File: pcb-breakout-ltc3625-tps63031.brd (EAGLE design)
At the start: 40 x 22.7 mm, 16 parts, among them IC1 LTC3625

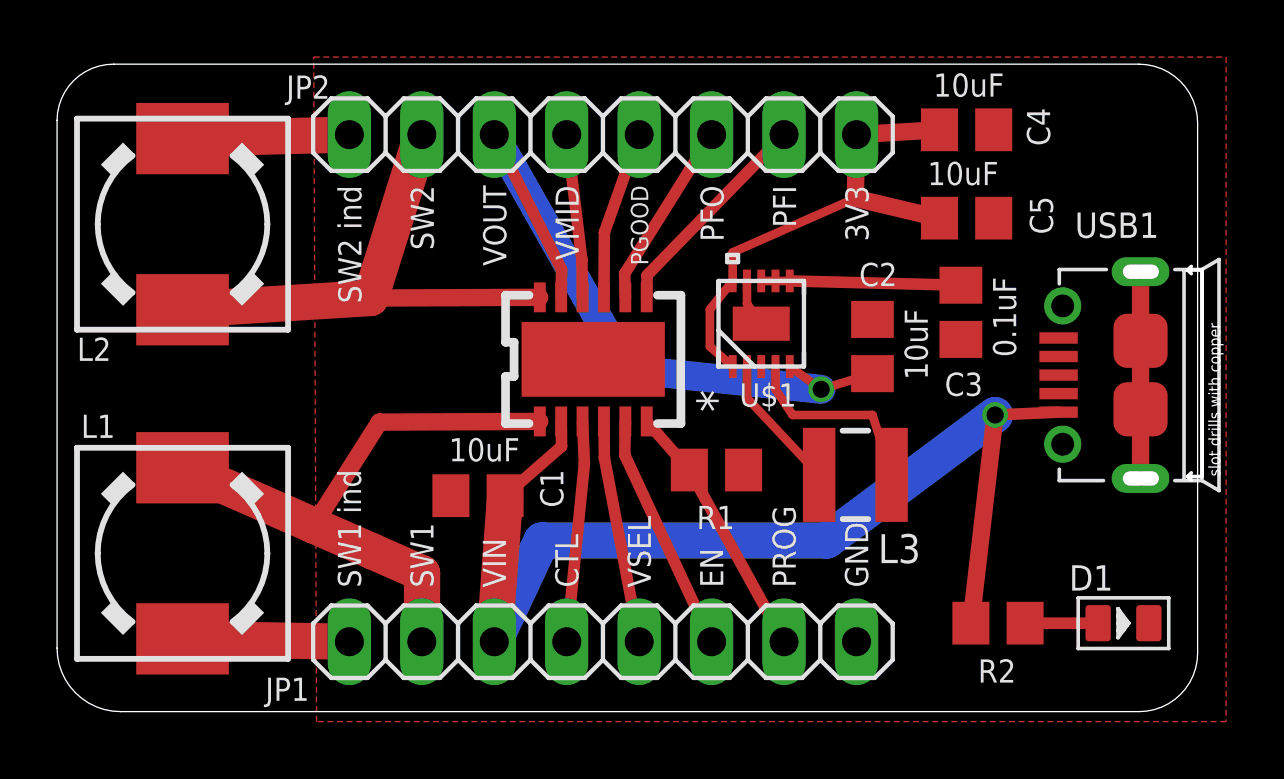
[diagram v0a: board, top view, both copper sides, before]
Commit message: corrected package error in ltc3625 lbr
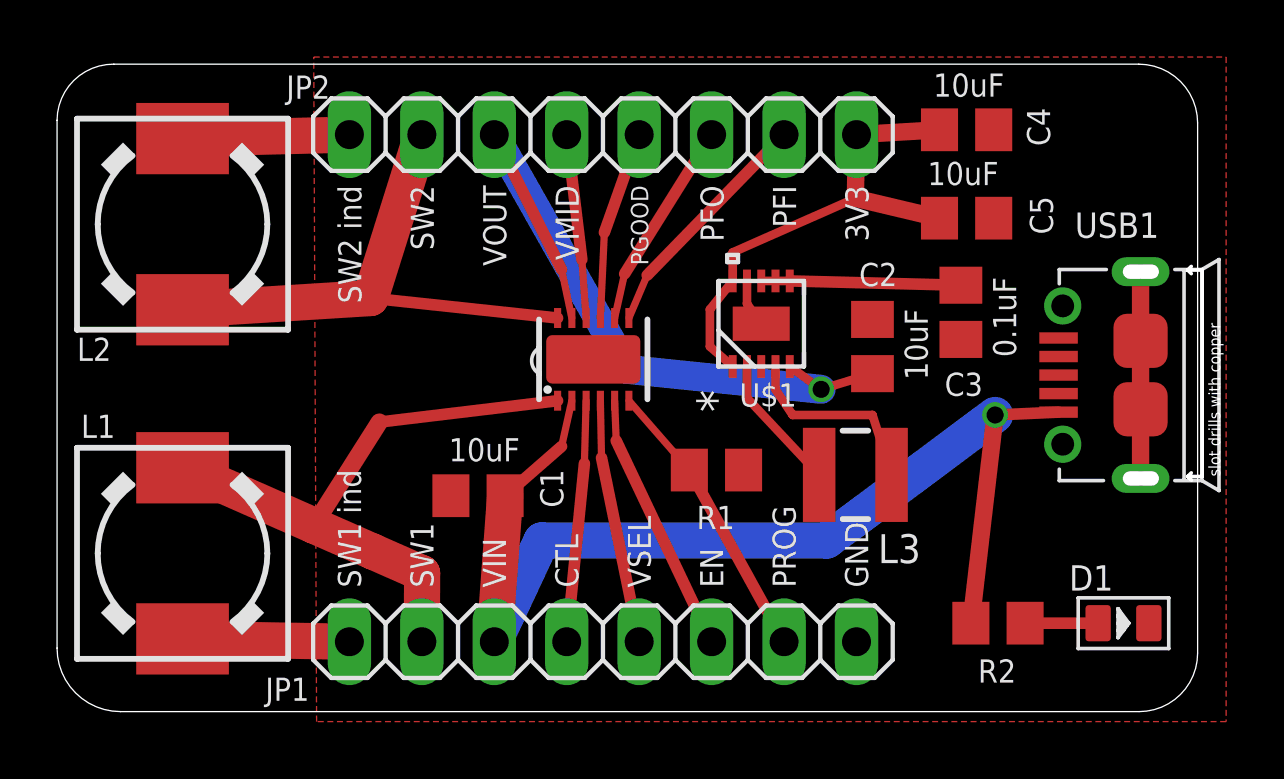
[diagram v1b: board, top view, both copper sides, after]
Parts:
- IC1: value LTC3625 -> LTC3625EDE
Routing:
- net L3625_PROG: track 9.14 -> 10.1 mm
- net L3625_PFI: track 7.66 -> 8.51 mm
- net L3625_EN: track 8.40 -> 9.20 mm
- net L3625_VIN: track 39.5 -> 40.3 mm
- net L3625_PFO: track 6.58 -> 7.34 mm
- net L3625_VOUT: track 25.8 -> 26.6 mm
- net L3625_VSEL: track 7.84 -> 8.58 mm
- net L3625_VMID: track 5.74 -> 6.47 mm
- net L3625_PGOOD: track 5.92 -> 6.64 mm
- net L3625_CTL: track 7.76 -> 8.48 mm
- net L3625_SW1: track 21.5 -> 22.2 mm
- net L3625_SW2: track 18.5 -> 19.2 mm
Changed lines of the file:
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@@
 <layer number="27" name="tValues" color="7" fill="1" visible="yes" active="yes"/>
 <layer number="28" name="bValues" color="7" fill="1" visible="yes" active="yes"/>
-<layer number="29" name="tStop" color="7" fill="3" visible="yes" active="yes"/>
-<layer number="30" name="bStop" color="7" fill="6" visible="yes" active="yes"/>
+<layer number="29" name="tStop" color="7" fill="3" visible="no" active="yes"/>
+<layer number="30" name="bStop" color="7" fill="6" visible="no" active="yes"/>
 <layer number="31" name="tCream" color="7" fill="4" visible="yes" active="yes"/>
 <layer number="32" name="bCream" color="7" fill="5" visible="yes" active="yes"/>
@@
 </autorouter>
 <elements>
-<element name="IC1" library="ltc3625" package="DFN12(DE)" value="LTC3625" x="18.81" y="12.35" smashed="yes">
+<element name="IC1" library="ltc3625" package="DFN12(DE)" value="LTC3625EDE" x="18.81" y="12.35" smashed="yes">
 <attribute name="NAME" x="14.9" y="12.67" size="1.016" layer="27" rot="R90" align="center"/>
 </element>
@@
 <wire x1="9.010409375" y1="6.523628125" x2="11.081146875" y2="5.61151875" width="1.27" layer="1"/>
 <wire x1="11.081146875" y1="5.61151875" x2="12.81" y2="4.85" width="1.27" layer="1"/>
-<wire x1="16.935" y1="10.175" x2="11.31" y2="10.15" width="0.6096" layer="1"/>
+<wire x1="17.56" y1="10.9" x2="11.31" y2="10.15" width="0.4064" layer="1"/>
 <wire x1="11.31" y1="10.15" x2="9.010409375" y2="6.523628125" width="0.6096" layer="1"/>
 <contactref element="JP1" pad="2"/>
@@
 <contactref element="IC1" pad="4"/>
 <contactref element="JP1" pad="5"/>
-<wire x1="19.185" y1="10.175" x2="19.2" y2="8.9" width="0.4064" layer="1"/>
-<wire x1="19.2" y1="8.9" x2="20.42" y2="2.45" width="0.4064" layer="1"/>
+<wire x1="19.06" y1="10.9" x2="19.1" y2="8.9" width="0.254" layer="1"/>
+<wire x1="19.1" y1="8.9" x2="20.42" y2="2.45" width="0.4064" layer="1"/>
 </signal>
 <signal name="L3625_PROG">
@@
 <contactref element="JP1" pad="7"/>
 <wire x1="22.18" y1="8.47" x2="25.5" y2="2.45" width="0.4064" layer="1"/>
-<wire x1="20.685" y1="10.175" x2="22.18" y2="8.47" width="0.4064" layer="1"/>
+<wire x1="20.06" y1="10.9" x2="22.18" y2="8.47" width="0.254" layer="1"/>
 </signal>
 <signal name="GND">
@@
 <signal name="L3625_EN">
 <contactref element="IC1" pad="5"/>
-<wire x1="19.935" y1="10.175" x2="19.91435" y2="8.99799375" width="0.4064" layer="1"/>
+<wire x1="19.56" y1="10.9" x2="19.61435" y2="9.49799375" width="0.254" layer="1"/>
 <contactref element="JP1" pad="6"/>
-<wire x1="19.91435" y1="8.99799375" x2="22.96" y2="2.45" width="0.4064" layer="1"/>
+<wire x1="19.61435" y1="9.49799375" x2="22.96" y2="2.45" width="0.4064" layer="1"/>
 </signal>
 <signal name="L3625_CTL">
 <contactref element="IC1" pad="3"/>
 <contactref element="JP1" pad="4"/>
-<wire x1="18.435" y1="10.175" x2="18.5" y2="8.7" width="0.4064" layer="1"/>
+<wire x1="18.56" y1="10.9" x2="18.5" y2="8.7" width="0.254" layer="1"/>
 <wire x1="18.5" y1="8.7" x2="17.88" y2="2.45" width="0.4064" layer="1"/>
 </signal>
@@
 <contactref element="JP2" pad="2"/>
 <contactref element="IC1" pad="7"/>
-<wire x1="20.685" y1="14.525" x2="20.7" y2="15.3" width="0.4064" layer="1"/>
+<wire x1="20.06" y1="13.8" x2="20.7" y2="15.3" width="0.254" layer="1"/>
 <wire x1="20.7" y1="15.3" x2="25.5" y2="20.23" width="0.4064" layer="1"/>
 </signal>
@@
 <contactref element="JP2" pad="3"/>
 <contactref element="IC1" pad="8"/>
-<wire x1="19.935" y1="14.525" x2="19.91" y2="15.35" width="0.4064" layer="1"/>
+<wire x1="19.56" y1="13.8" x2="19.91" y2="15.35" width="0.254" layer="1"/>
 <wire x1="19.91" y1="15.35" x2="22.96" y2="20.23" width="0.4064" layer="1"/>
 </signal>
@@
 <contactref element="JP2" pad="4"/>
 <contactref element="IC1" pad="9"/>
-<wire x1="19.185" y1="14.525" x2="19.2" y2="16.8" width="0.4064" layer="1"/>
+<wire x1="19.06" y1="13.8" x2="19.2" y2="16.8" width="0.254" layer="1"/>
 <wire x1="19.2" y1="16.8" x2="20.42" y2="20.23" width="0.4064" layer="1"/>
 </signal>
@@
 <contactref element="JP2" pad="5"/>
 <contactref element="IC1" pad="10"/>
-<wire x1="18.435" y1="14.525" x2="18.41" y2="15.85" width="0.4064" layer="1"/>
+<wire x1="18.56" y1="13.8" x2="18.41" y2="15.85" width="0.254" layer="1"/>
 <wire x1="18.41" y1="15.85" x2="17.88" y2="20.23" width="0.4064" layer="1"/>
 </signal>
@@
 <contactref element="JP2" pad="6"/>
 <contactref element="IC1" pad="11"/>
-<wire x1="17.685" y1="14.525" x2="17.7" y2="15.5" width="0.4064" layer="1"/>
+<wire x1="18.06" y1="13.8" x2="17.7" y2="15.5" width="0.254" layer="1"/>
 <wire x1="17.7" y1="15.5" x2="15.34" y2="20.23" width="0.4064" layer="1"/>
 <contactref element="U$1" pad="5"/>
@@
 <wire x1="4.41" y1="14.09" x2="11" y2="14.5" width="1.27" layer="1"/>
 <wire x1="11" y1="14.5" x2="12.8" y2="20.23" width="1.27" layer="1"/>
-<wire x1="16.935" y1="14.525" x2="11" y2="14.5" width="0.6096" layer="1"/>
+<wire x1="17.56" y1="13.8" x2="11" y2="14.5" width="0.4064" layer="1"/>
 </signal>
 <signal name="L3625_SW2_IND">
@@
 <wire x1="35.125" y1="10.5" x2="32.9" y2="10.4" width="0.4064" layer="1"/>
 <wire x1="15.34" y1="2.45" x2="15.72" y2="7.57" width="1.27" layer="1"/>
-<wire x1="17.685" y1="10.175" x2="17.7" y2="9.3" width="0.4064" layer="1"/>
+<wire x1="18.06" y1="10.9" x2="17.7" y2="9.3" width="0.254" layer="1"/>
 <wire x1="17.7" y1="9.3" x2="15.72" y2="7.57" width="0.4064" layer="1"/>
 <via x="32.9" y="10.4" extent="1-16" drill="0.6" shape="square"/>

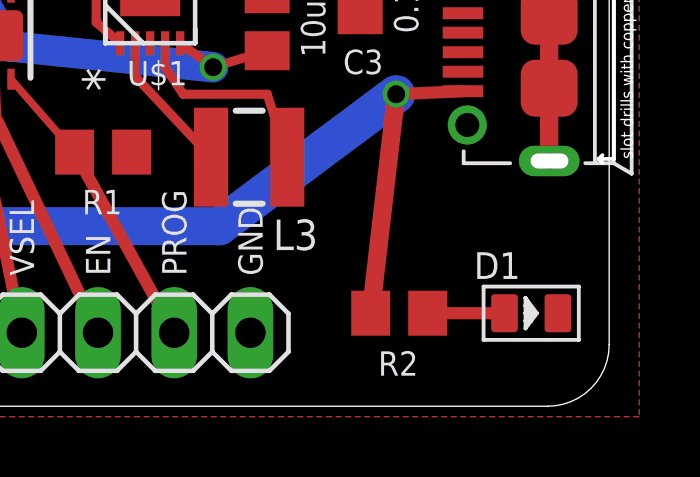
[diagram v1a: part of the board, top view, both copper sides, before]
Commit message: 2kohm for led resistor value
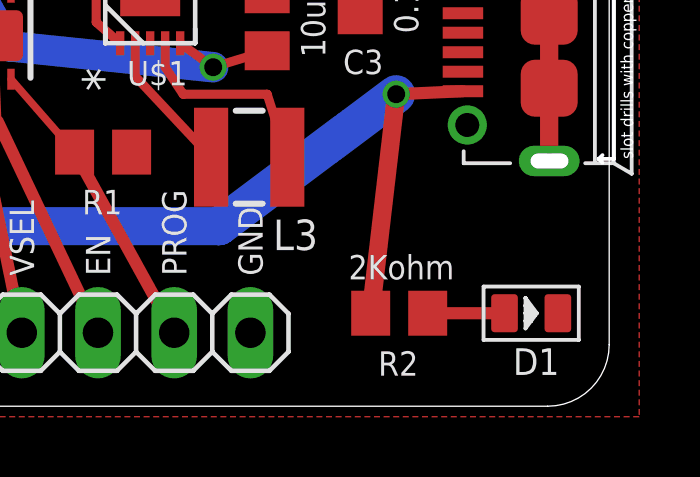
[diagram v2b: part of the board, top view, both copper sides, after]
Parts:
- R2: value (none) -> 2Kohm
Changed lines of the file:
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@@
 <attribute name="VALUE" x="30.53" y="18.46" size="0.8128" layer="21"/>
 </element>
-<element name="R2" library="resistor" package="R0805" value="" x="33" y="3.1" smashed="yes" rot="R180">
+<element name="R2" library="resistor" package="R0805" value="2Kohm" x="33" y="3.1" smashed="yes" rot="R180">
 <attribute name="NAME" x="33.635" y="1.83" size="0.8128" layer="25" rot="R180"/>
-<attribute name="VALUE" x="33.635" y="5.64" size="1.27" layer="27" rot="R180"/>
+<attribute name="VALUE" x="34.835" y="5.04" size="0.8128" layer="21" rot="R180"/>
 </element>
 <element name="D1" library="Seeed-OPL-Diode" package="LED-0805" value="YELLOW-0805" x="37.4" y="3.1" smashed="yes">
 <attribute name="MPN" value="17-215UYC/S530-A3/TR8" x="37.4" y="3.1" size="1.778" layer="27" display="off"/>
-<attribute name="NAME" x="35.495" y="4.243" size="0.889" layer="25" font="vector" ratio="11"/>
+<attribute name="NAME" x="36.795" y="1.043" size="0.889" layer="25" font="vector" ratio="11"/>
 </element>
 </elements>

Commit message: adjust positioning
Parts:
- moved R1 5.95 mm to (17.7, 11.0), turned to 270 degrees
- moved IC1 4.41 mm to (14.4, 12.4)
- moved C1 2.00 mm to (12.8, 7.57)
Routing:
- net L3625_SW1: track 22.2 -> 17.3 mm
- net L3625_SW2: track 19.2 -> 14.9 mm
- net L3625_PFI: track 8.51 -> 12.1 mm
- net L3625_PFO: track 7.34 -> 10.8 mm
- net L3625_PROG: track 10.1 -> 13.1 mm
- net L3625_EN: track 9.20 -> 11.8 mm
- net L3625_PGOOD: track 6.64 -> 8.92 mm
- net L3625_VSEL: track 8.58 -> 10.5 mm
- net L3625_VMID: track 6.47 -> 7.67 mm
- net L3625_CTL: track 8.48 -> 9.40 mm
- net L3625_VIN: track 40.3 -> 39.6 mm
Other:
- board text added: "LTC_EN"
- board text removed: "EN"
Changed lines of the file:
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@@
 <setting verticaltext="up"/>
 </settings>
-<grid distance="1" unitdist="mm" unit="mm" style="lines" multiple="1" display="yes" altdistance="0.1" altunitdist="mm" altunit="mm"/>
+<grid distance="1" unitdist="mm" unit="mm" style="lines" multiple="1" display="yes" altdistance="0.05" altunitdist="mm" altunit="mm"/>
 <layers>
 <layer number="1" name="Top" color="4" fill="1" visible="yes" active="yes"/>
@@
 <layer number="20" name="Dimension" color="15" fill="1" visible="yes" active="yes"/>
 <layer number="21" name="tPlace" color="7" fill="1" visible="yes" active="yes"/>
-<layer number="22" name="bPlace" color="7" fill="1" visible="yes" active="yes"/>
+<layer number="22" name="bPlace" color="7" fill="1" visible="no" active="yes"/>
 <layer number="23" name="tOrigins" color="15" fill="1" visible="yes" active="yes"/>
 <layer number="24" name="bOrigins" color="15" fill="1" visible="yes" active="yes"/>
@@
 <text x="18.29" y="4.35" size="0.8128" layer="21" rot="R90">CTL</text>
 <text x="20.83" y="4.35" size="0.8128" layer="21" rot="R90">VSEL</text>
-<text x="23.37" y="4.35" size="0.8128" layer="21" rot="R90">EN</text>
+<text x="23.37" y="4.35" size="0.8128" layer="21" rot="R90">LTC_EN</text>
 <text x="25.91" y="4.35" size="0.8128" layer="21" rot="R90">PROG</text>
 <text x="25.11" y="18.45" size="0.8128" layer="21" rot="R270">PFI</text>
@@
 </autorouter>
 <elements>
-<element name="IC1" library="ltc3625" package="DFN12(DE)" value="LTC3625EDE" x="18.81" y="12.35" smashed="yes">
-<attribute name="NAME" x="14.9" y="12.67" size="1.016" layer="27" rot="R90" align="center"/>
+<element name="IC1" library="ltc3625" package="DFN12(DE)" value="LTC3625EDE" x="14.4" y="12.4" smashed="yes">
+<attribute name="NAME" x="10.49" y="12.72" size="1.016" layer="27" rot="R90" align="center"/>
 </element>
 <element name="JP1" library="pinhead" package="1X08" value="" x="19.15" y="2.45" smashed="yes">
@@
 <attribute name="VALUE" x="29.31" y="23.405" size="1.27" layer="27" rot="R180"/>
 </element>
-<element name="C1" library="rcl" package="C0805" value="10uF" x="14.77" y="7.57" smashed="yes" rot="R180">
-<attribute name="NAME" x="16.95" y="8.49" size="0.8128" layer="25" rot="R270"/>
-<attribute name="VALUE" x="13.745" y="8.775" size="0.8128" layer="21"/>
-</element>
-<element name="R1" library="resistor" package="R0805" value="" x="23.13" y="8.47" smashed="yes" rot="R180">
-<attribute name="NAME" x="22.435" y="6.4" size="0.8128" layer="25"/>
-<attribute name="VALUE" x="23.765" y="11.01" size="1.27" layer="27" rot="R180"/>
+<element name="C1" library="rcl" package="C0805" value="10uF" x="12.77" y="7.57" smashed="yes" rot="R180">
+<attribute name="NAME" x="14.95" y="8.49" size="0.8128" layer="25" rot="R270"/>
+<attribute name="VALUE" x="11.745" y="8.775" size="0.8128" layer="21"/>
+</element>
+<element name="R1" library="resistor" package="R0805" value="" x="17.73" y="10.98" smashed="yes" rot="R270">
+<attribute name="NAME" x="18.565" y="8.7" size="0.8128" layer="25" rot="R180"/>
+<attribute name="VALUE" x="15.19" y="11.615" size="1.27" layer="27" rot="R270"/>
 </element>
 <element name="L1" library="inductors" package="DR73" value="3.3uH" x="4.41" y="5.55" smashed="yes" rot="R90">
@@
 <contactref element="L1" pad="2"/>
 <wire x1="4.41" y1="8.55" x2="9.010409375" y2="6.523628125" width="1.27" layer="1"/>
-<wire x1="9.010409375" y1="6.523628125" x2="11.081146875" y2="5.61151875" width="1.27" layer="1"/>
-<wire x1="11.081146875" y1="5.61151875" x2="12.81" y2="4.85" width="1.27" layer="1"/>
-<wire x1="17.56" y1="10.9" x2="11.31" y2="10.15" width="0.4064" layer="1"/>
+<wire x1="9.010409375" y1="6.523628125" x2="10.681146875" y2="5.71151875" width="1.27" layer="1"/>
+<wire x1="10.681146875" y1="5.71151875" x2="11.81" y2="5.15" width="1.27" layer="1"/>
+<wire x1="13.15" y1="10.95" x2="11.31" y2="10.15" width="0.4064" layer="1"/>
 <wire x1="11.31" y1="10.15" x2="9.010409375" y2="6.523628125" width="0.6096" layer="1"/>
 <contactref element="JP1" pad="2"/>
-<wire x1="12.81" y1="4.85" x2="12.8" y2="2.45" width="1.27" layer="1"/>
+<wire x1="11.81" y1="5.15" x2="12.8" y2="2.45" width="1.27" layer="1"/>
 </signal>
 <signal name="L3625_VSEL">
 <contactref element="IC1" pad="4"/>
 <contactref element="JP1" pad="5"/>
-<wire x1="19.06" y1="10.9" x2="19.1" y2="8.9" width="0.254" layer="1"/>
-<wire x1="19.1" y1="8.9" x2="20.42" y2="2.45" width="0.4064" layer="1"/>
+<wire x1="14.65" y1="10.95" x2="14.65" y2="9.9" width="0.254" layer="1"/>
+<wire x1="14.65" y1="9.9" x2="20.42" y2="2.45" width="0.3048" layer="1"/>
 </signal>
 <signal name="L3625_PROG">
@@
 <contactref element="R1" pad="2"/>
 <contactref element="JP1" pad="7"/>
-<wire x1="22.18" y1="8.47" x2="25.5" y2="2.45" width="0.4064" layer="1"/>
-<wire x1="20.06" y1="10.9" x2="22.18" y2="8.47" width="0.254" layer="1"/>
+<wire x1="17.73" y1="10.03" x2="25.5" y2="2.45" width="0.4064" layer="1"/>
+<wire x1="15.65" y1="10.95" x2="17.73" y2="10.03" width="0.254" layer="1"/>
 </signal>
 <signal name="GND">
@@
 <signal name="L3625_EN">
 <contactref element="IC1" pad="5"/>
-<wire x1="19.56" y1="10.9" x2="19.61435" y2="9.49799375" width="0.254" layer="1"/>
+<wire x1="15.15" y1="10.95" x2="15.16435" y2="10.14799375" width="0.254" layer="1"/>
 <contactref element="JP1" pad="6"/>
-<wire x1="19.61435" y1="9.49799375" x2="22.96" y2="2.45" width="0.4064" layer="1"/>
+<wire x1="15.16435" y1="10.14799375" x2="22.96" y2="2.45" width="0.3048" layer="1"/>
 </signal>
 <signal name="L3625_CTL">
 <contactref element="IC1" pad="3"/>
 <contactref element="JP1" pad="4"/>
-<wire x1="18.56" y1="10.9" x2="18.5" y2="8.7" width="0.254" layer="1"/>
-<wire x1="18.5" y1="8.7" x2="17.88" y2="2.45" width="0.4064" layer="1"/>
+<wire x1="14.15" y1="10.95" x2="14.15" y2="9.7" width="0.254" layer="1"/>
+<wire x1="14.15" y1="9.7" x2="17.88" y2="2.45" width="0.3048" layer="1"/>
 </signal>
 <signal name="L3625_SW1_IND">
@@
 <contactref element="JP2" pad="2"/>
 <contactref element="IC1" pad="7"/>
-<wire x1="20.06" y1="13.8" x2="20.7" y2="15.3" width="0.254" layer="1"/>
-<wire x1="20.7" y1="15.3" x2="25.5" y2="20.23" width="0.4064" layer="1"/>
+<wire x1="15.65" y1="13.85" x2="21.15" y2="15.65" width="0.254" layer="1"/>
+<wire x1="21.15" y1="15.65" x2="25.5" y2="20.23" width="0.3048" layer="1"/>
 </signal>
 <signal name="L3625_PFO">
 <contactref element="JP2" pad="3"/>
 <contactref element="IC1" pad="8"/>
-<wire x1="19.56" y1="13.8" x2="19.91" y2="15.35" width="0.254" layer="1"/>
-<wire x1="19.91" y1="15.35" x2="22.96" y2="20.23" width="0.4064" layer="1"/>
+<wire x1="15.15" y1="13.85" x2="15.16" y2="14.55" width="0.254" layer="1"/>
+<wire x1="22" y1="18" x2="22.96" y2="20.23" width="0.254" layer="1"/>
+<wire x1="15.16" y1="14.55" x2="16" y2="15" width="0.254" layer="1"/>
+<wire x1="16" y1="15" x2="22" y2="18" width="0.3048" layer="1"/>
 </signal>
 <signal name="L3625_PGOOD">
 <contactref element="JP2" pad="4"/>
 <contactref element="IC1" pad="9"/>
-<wire x1="19.06" y1="13.8" x2="19.2" y2="16.8" width="0.254" layer="1"/>
-<wire x1="19.2" y1="16.8" x2="20.42" y2="20.23" width="0.4064" layer="1"/>
+<wire x1="14.65" y1="13.85" x2="14.65" y2="14.95" width="0.254" layer="1"/>
+<wire x1="14.65" y1="14.95" x2="20.42" y2="20.23" width="0.3048" layer="1"/>
 </signal>
 <signal name="L3625_VMID">
 <contactref element="JP2" pad="5"/>
 <contactref element="IC1" pad="10"/>
-<wire x1="18.56" y1="13.8" x2="18.41" y2="15.85" width="0.254" layer="1"/>
-<wire x1="18.41" y1="15.85" x2="17.88" y2="20.23" width="0.4064" layer="1"/>
+<wire x1="14.15" y1="13.85" x2="14.11" y2="15.35" width="0.254" layer="1"/>
+<wire x1="14.11" y1="15.35" x2="17.88" y2="20.23" width="0.3048" layer="1"/>
 </signal>
 <signal name="L3625_VOUT">
 <contactref element="JP2" pad="6"/>
 <contactref element="IC1" pad="11"/>
-<wire x1="18.06" y1="13.8" x2="17.7" y2="15.5" width="0.254" layer="1"/>
-<wire x1="17.7" y1="15.5" x2="15.34" y2="20.23" width="0.4064" layer="1"/>
+<wire x1="13.65" y1="13.85" x2="13.65" y2="18.1" width="0.254" layer="1"/>
+<wire x1="13.65" y1="18.1" x2="15.34" y2="20.23" width="0.3048" layer="1"/>
 <contactref element="U$1" pad="5"/>
 <contactref element="C2" pad="1"/>
@@
 <wire x1="4.41" y1="14.09" x2="11" y2="14.5" width="1.27" layer="1"/>
 <wire x1="11" y1="14.5" x2="12.8" y2="20.23" width="1.27" layer="1"/>
-<wire x1="17.56" y1="13.8" x2="11" y2="14.5" width="0.4064" layer="1"/>
+<wire x1="13.15" y1="13.85" x2="11" y2="14.5" width="0.4064" layer="1"/>
 </signal>
 <signal name="L3625_SW2_IND">
@@
 <contactref element="JP1" pad="3"/>
 <wire x1="35.125" y1="10.5" x2="32.9" y2="10.4" width="0.4064" layer="1"/>
-<wire x1="15.34" y1="2.45" x2="15.72" y2="7.57" width="1.27" layer="1"/>
-<wire x1="18.06" y1="10.9" x2="17.7" y2="9.3" width="0.254" layer="1"/>
-<wire x1="17.7" y1="9.3" x2="15.72" y2="7.57" width="0.4064" layer="1"/>
+<wire x1="15.34" y1="2.45" x2="13.72" y2="7.57" width="0.8128" layer="1"/>
 <via x="32.9" y="10.4" extent="1-16" drill="0.6" shape="square"/>
 <wire x1="32.9" y1="10.4" x2="27" y2="6" width="1.27" layer="16"/>
@@
 <wire x1="17" y1="6" x2="15.34" y2="2.45" width="1.27" layer="16"/>
 <wire x1="32.05" y1="3.1" x2="32.9" y2="10.4" width="0.6096" layer="1"/>
+<wire x1="13.65" y1="10.95" x2="13.72" y2="7.57" width="0.254" layer="1"/>
 </signal>
 </signals>
